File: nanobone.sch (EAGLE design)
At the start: 44 parts, among them J1 USD_CONNECTOR, U1 24LC_32AT-I/OT, U2 OSD3358, U3 SN74LVC1G07_DCK_5, U4 AR8035-AL1B, Y1 CM200C-32.768KAZF-UT, Y2 445C33D24M00000

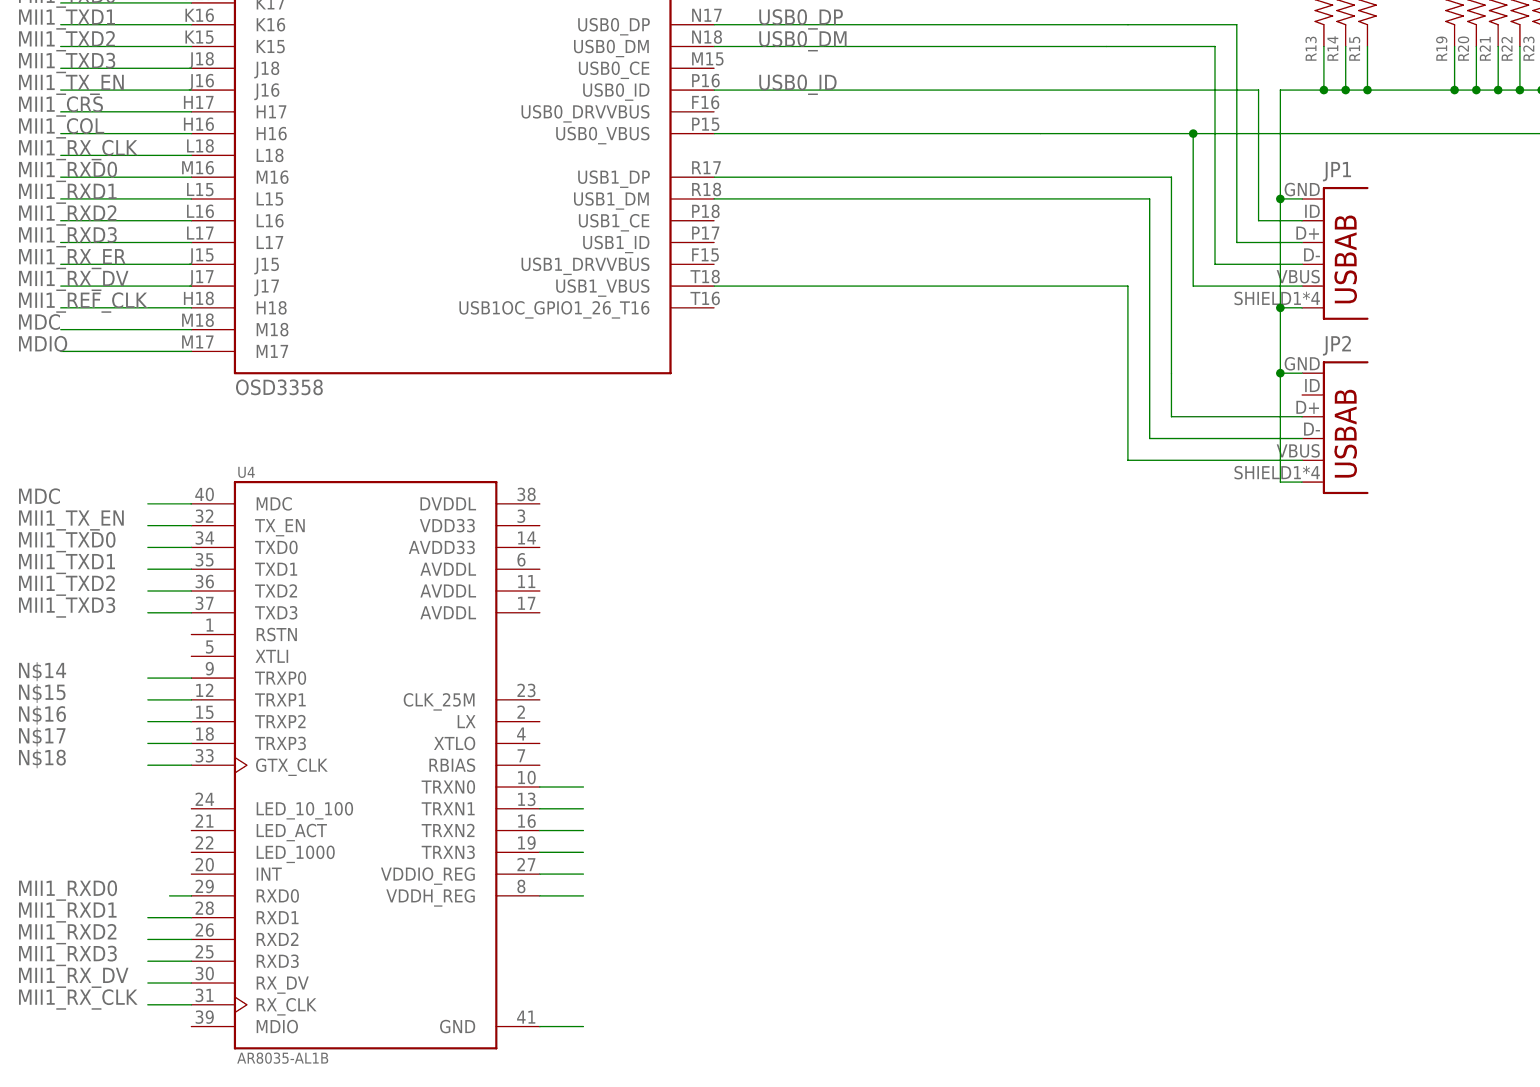
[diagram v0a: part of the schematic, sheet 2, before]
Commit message: Removed AR8035 due to lack of space and routing issues. Centered crystals in pocketbone.lbr and renamed to nanobone.lbr
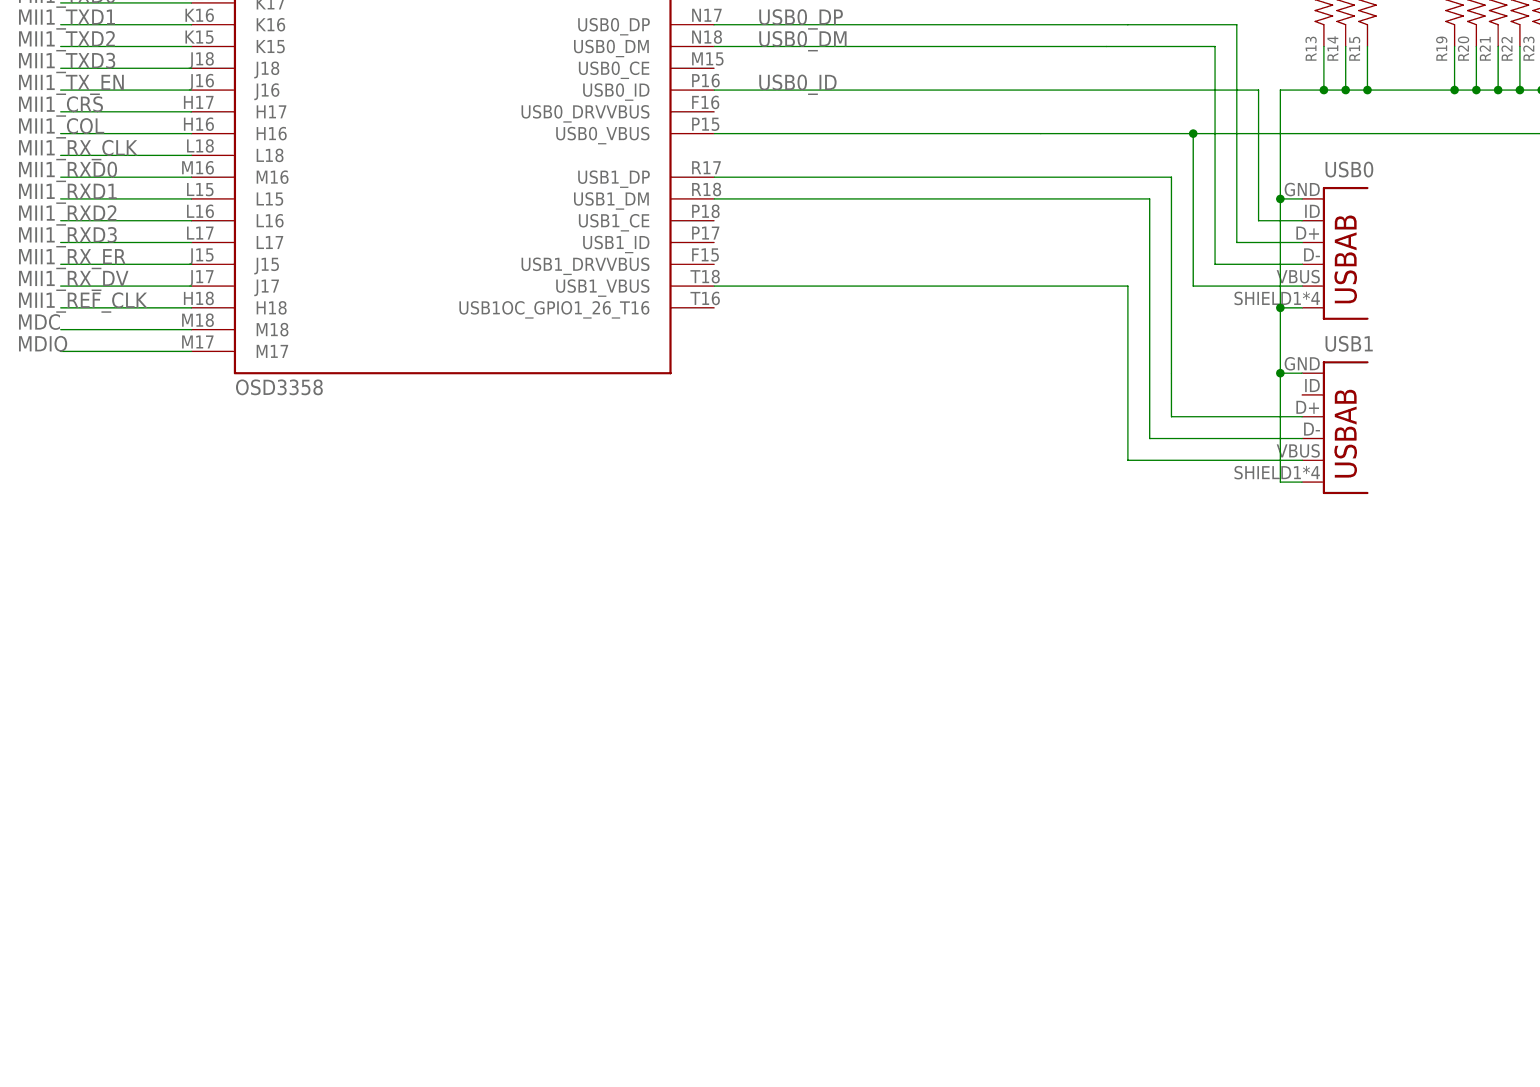
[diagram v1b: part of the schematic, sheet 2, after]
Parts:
- removed U4: AR8035-AL1B, AR8035-AL1B:AR8035-AL1B
- renumbered JP1 to USB0, JP2 to USB1
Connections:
- removed net N$14: U4.TRXP0
- removed net N$15: U4.TRXP1
- removed net N$16: U4.TRXP2
- removed net N$17: U4.TRXP3
- removed net N$18: U4.GTX_CLK
- removed net N$19: U4.TRXN0
- removed net N$20: U4.TRXN1
- removed net N$21: U4.TRXN2
- removed net N$22: U4.TRXN3
- removed net N$23: U4.VDDIO_REG
- removed net N$24: U4.VDDH_REG
- removed net N$7: U4.GND
- net MDC: no longer U4.MDC
- net MII1_RXD0: no longer U4.RXD0
- net MII1_RXD1: no longer U4.RXD1
- net MII1_RXD2: no longer U4.RXD2
- net MII1_RXD3: no longer U4.RXD3
- net MII1_RX_CLK: no longer U4.RX_CLK
- net MII1_RX_DV: no longer U4.RX_DV
- net MII1_TXD0: no longer U4.TXD0
- net MII1_TXD1: no longer U4.TXD1
- net MII1_TXD2: no longer U4.TXD2
- net MII1_TXD3: no longer U4.TXD3
- net MII1_TX_EN: no longer U4.TX_EN

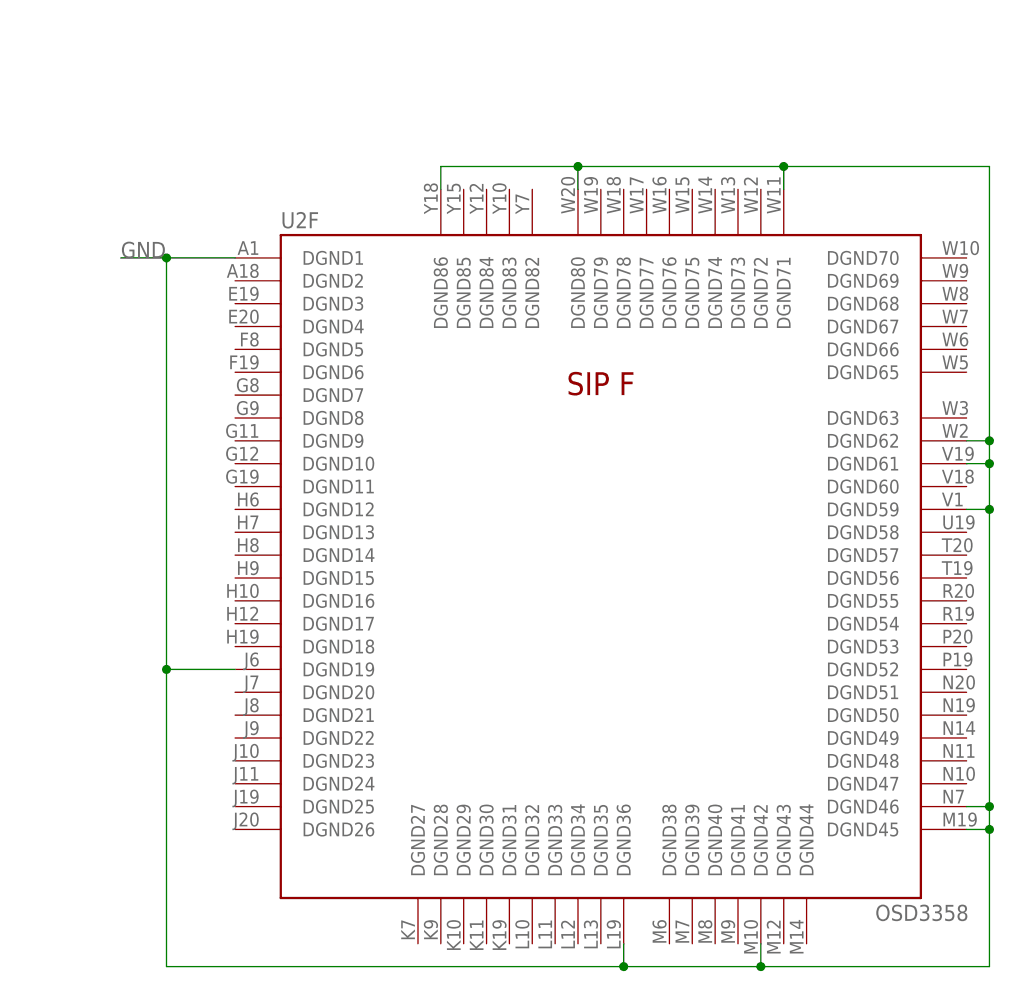
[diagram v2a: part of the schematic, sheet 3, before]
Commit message: Remove PHY nets from schematic. Tie all DGND to GND plane. Improve USB differential pair isolation.
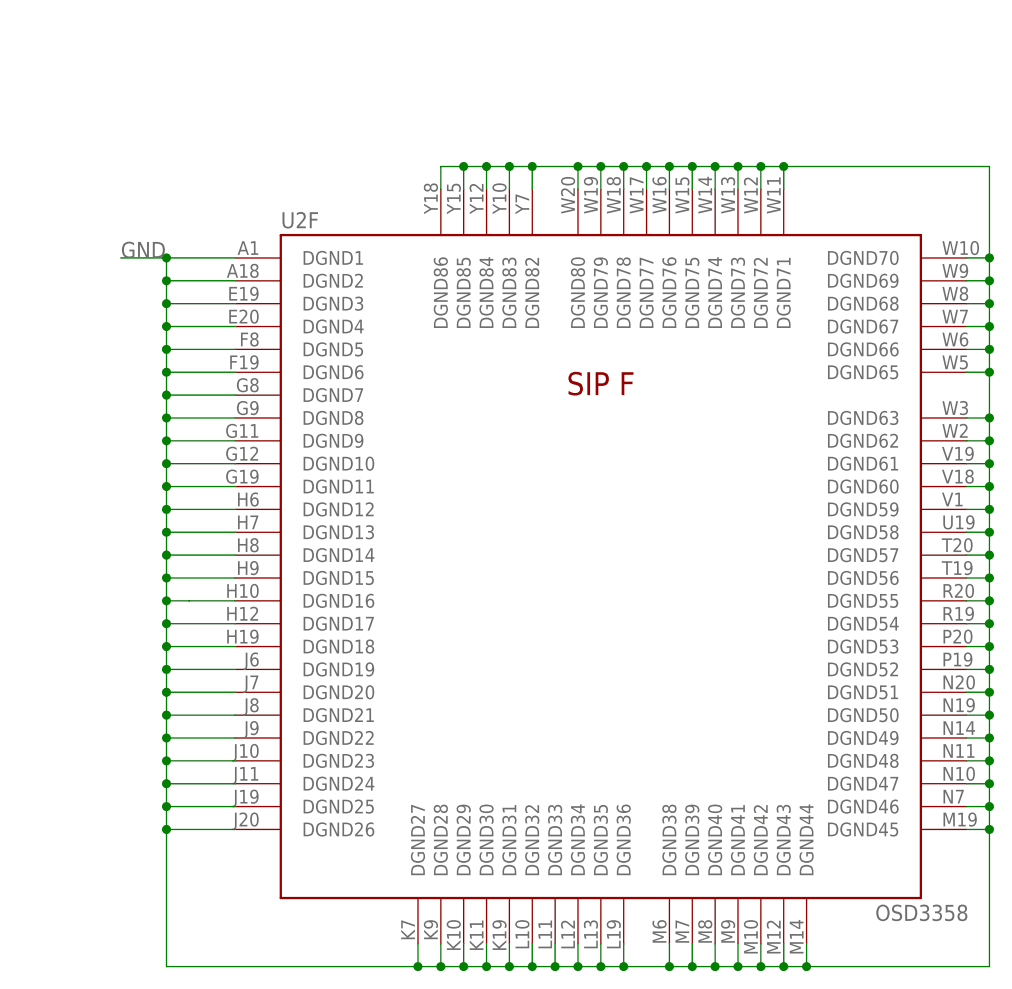
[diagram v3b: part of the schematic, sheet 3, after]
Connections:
- removed net 5.0V: U2A.VIN_AC_0, U2A.VIN_AC_1
- removed net MDC: U2C.M18
- removed net MDIO: U2C.M17
- removed net MII1_COL: U2C.H16
- removed net MII1_CRS: U2C.H17
- removed net MII1_REF_CLK: U2C.H18
- removed net MII1_RXD0: U2C.M16
- removed net MII1_RXD1: U2C.L15
- removed net MII1_RXD2: U2C.L16
- removed net MII1_RXD3: U2C.L17
- removed net MII1_RX_CLK: U2C.L18
- removed net MII1_RX_DV: U2C.J17
- removed net MII1_RX_ER: U2C.J15
- removed net MII1_TXD0: U2C.K17
- removed net MII1_TXD1: U2C.K16
- removed net MII1_TXD2: U2C.K15
- removed net MII1_TXD3: U2C.J18
- removed net MII1_TX_CLK: U2C.K18
- removed net MII1_TX_EN: U2C.J16
- net GND: now also U2F.DGND10, U2F.DGND11, U2F.DGND12, U2F.DGND13, U2F.DGND14, U2F.DGND15, U2F.DGND16, U2F.DGND17, U2F.DGND18, U2F.DGND2, U2F.DGND20, U2F.DGND21, U2F.DGND22, U2F.DGND23, U2F.DGND24, U2F.DGND25, U2F.DGND26, U2F.DGND27, U2F.DGND28, U2F.DGND29, U2F.DGND3, U2F.DGND30, U2F.DGND31, U2F.DGND32, U2F.DGND33, U2F.DGND34, U2F.DGND35, U2F.DGND38, U2F.DGND39, U2F.DGND4, U2F.DGND40, U2F.DGND41, U2F.DGND43, U2F.DGND44, U2F.DGND47, U2F.DGND48, U2F.DGND49, U2F.DGND5, U2F.DGND50, U2F.DGND51, U2F.DGND52, U2F.DGND53, U2F.DGND54, U2F.DGND55, U2F.DGND56, U2F.DGND57, U2F.DGND58, U2F.DGND6, U2F.DGND60, U2F.DGND63, U2F.DGND65, U2F.DGND66, U2F.DGND67, U2F.DGND68, U2F.DGND69, U2F.DGND7, U2F.DGND70, U2F.DGND72, U2F.DGND73, U2F.DGND74, U2F.DGND75, U2F.DGND76, U2F.DGND77, U2F.DGND78, U2F.DGND79, U2F.DGND8, U2F.DGND82, U2F.DGND83, U2F.DGND84, U2F.DGND85, U2F.DGND9

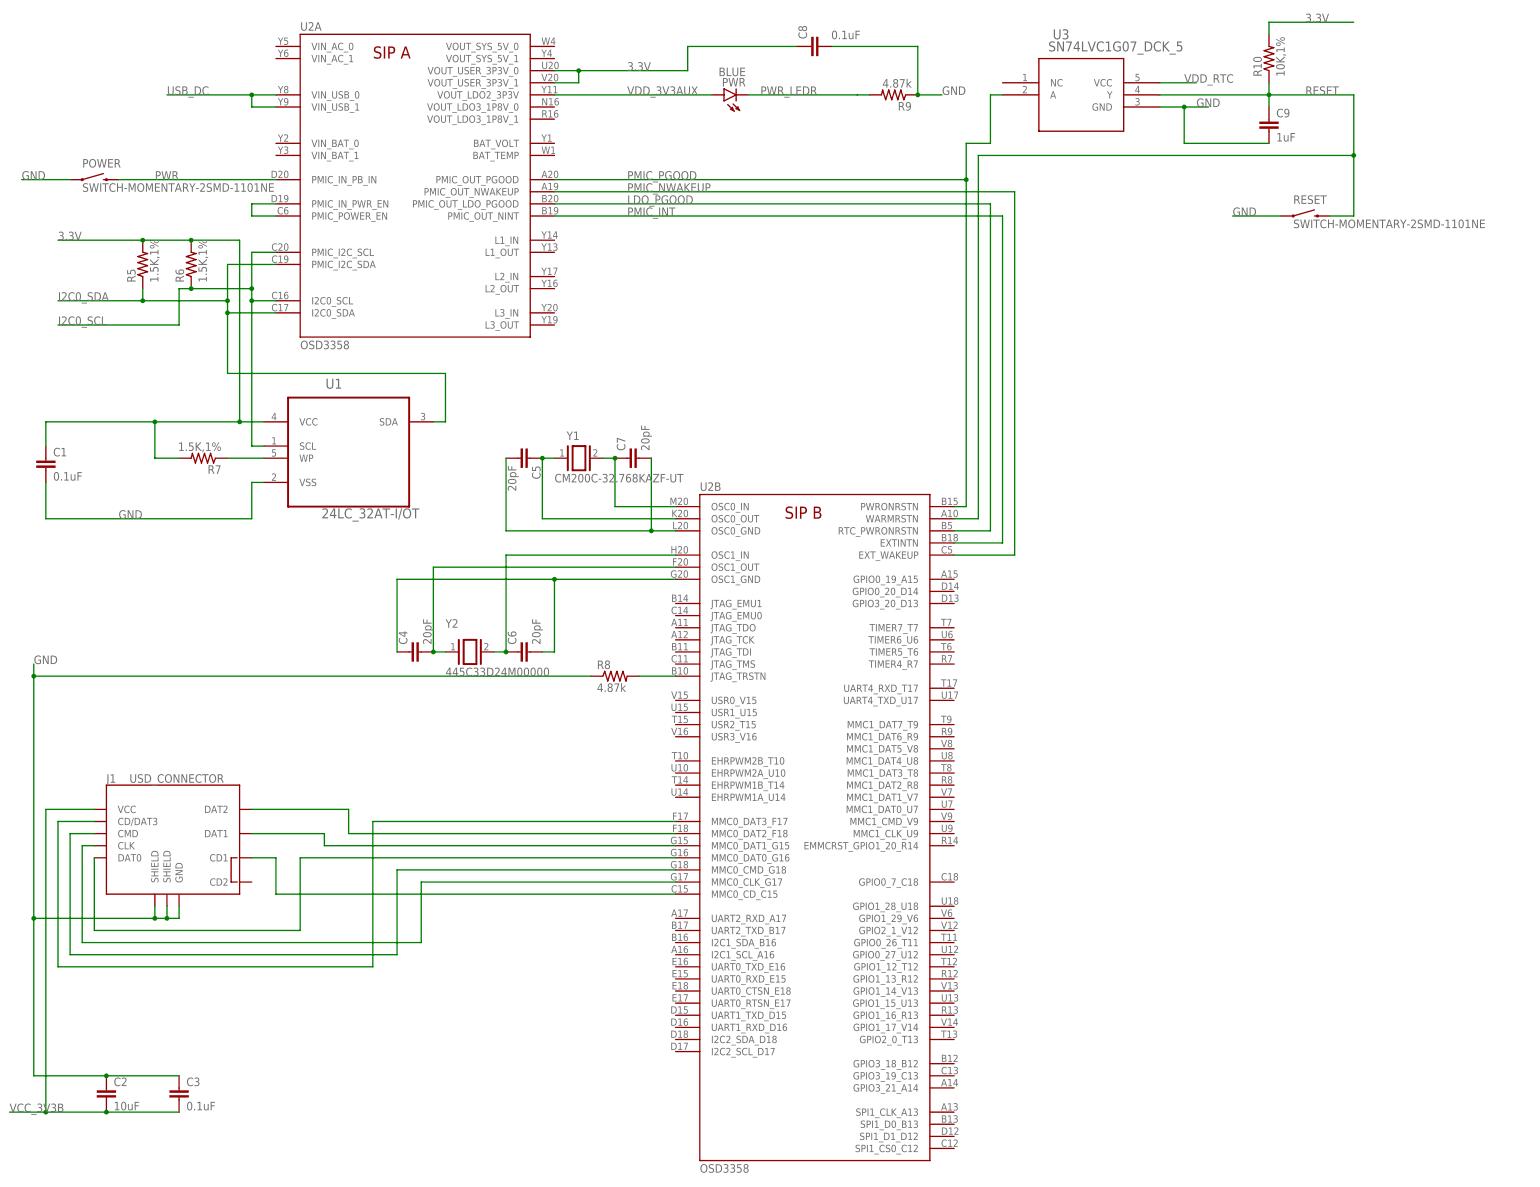
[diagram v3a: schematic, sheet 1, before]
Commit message: Cleaned layout further, added USB1_ID, added user LEDs
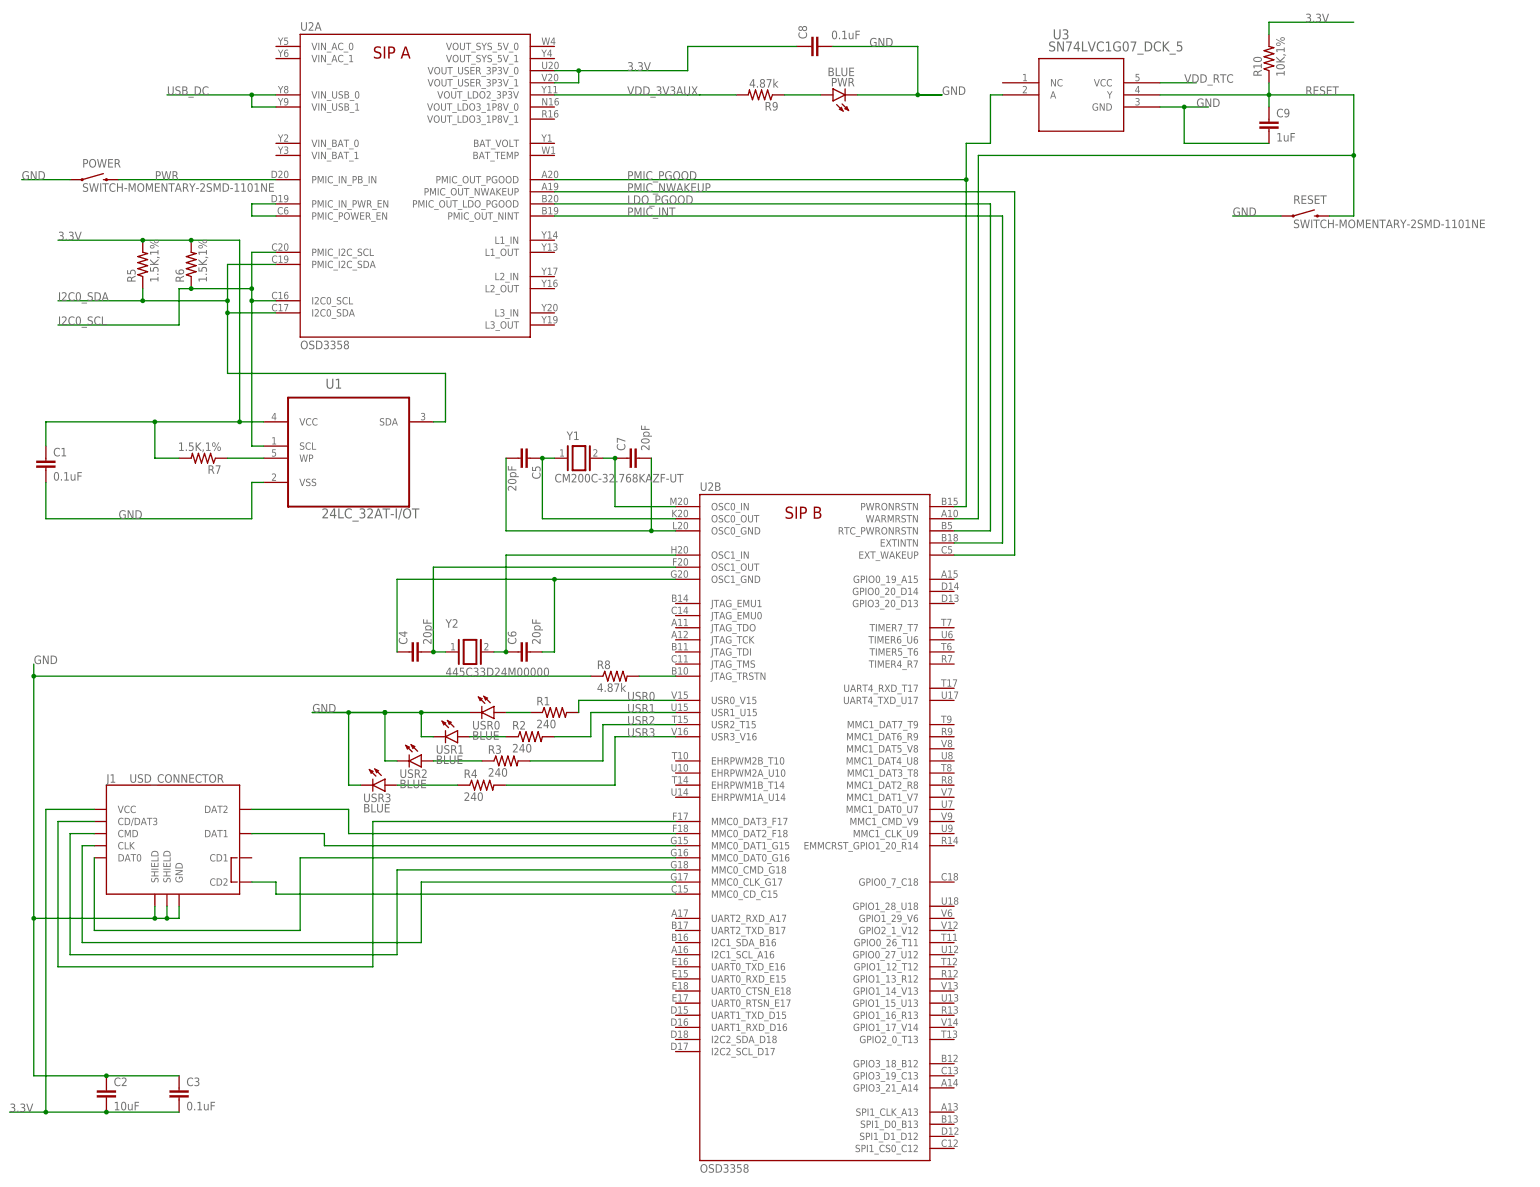
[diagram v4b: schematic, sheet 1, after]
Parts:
- added R1, R2, R3, R4: 240, Strawson_Eagle_Lib:RESISTOR0402-RES
- added USR0, USR1, USR2, USR3: BLUE, nanobone:LED0402
- PWR: device BeagleBone_Blue:LED0603 -> nanobone:LED0402
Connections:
- removed net PWR_LEDR: PWR.C, R9.2
- removed net VCC_3V3B: C2.2, C3.2, J1.VCC
- new net N$10: R3.1, USR2.A
- new net N$11: R4.1, USR3.A
- new net N$13: PWR.A, R9.1
- new net N$8: R1.1, USR0.A
- new net N$9: R2.1, USR1.A
- new net USB1_ID: U2C.USB1_ID, USB1.USBID
- new net USR0: R1.2, U2B.USR0_V15
- new net USR1: R2.2, U2B.USR1_U15
- new net USR2: R3.2, U2B.USR2_T15
- new net USR3: R4.2, U2B.USR3_V16
- net 3.3V: now also C2.2, C3.2, J1.VCC
- net GND: now also PWR.C, USR0.C, USR1.C, USR2.C, USR3.C; no longer R9.1
- net N$75: now also J1.CD2; no longer J1.CD1
- net VDD_3V3AUX: now also R9.2; no longer PWR.A
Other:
- moved on the sheet: R9
